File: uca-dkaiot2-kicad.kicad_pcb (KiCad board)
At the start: 2 copper layers, 73 x 77.5 mm, 184 parts, among them J1 Conn_01x04, J10 Conn_Coaxial, J11 Conn_01x02, J12 Conn_01x02, J20 Conn_01x01, J21 Conn_01x01, J22 Conn_01x01, J23 Conn_01x01, J24 Conn_01x01, J25 Conn_01x01, J26 Conn_01x01, J2J14 Conn_02x06_Odd_Even, J3 Conn_01x02, J4 Conn_01x02, J5 Conn_01x02, J6 Conn_Coaxial, J7 Conn_01x05, J8 USB_B_Micro, J9J13 Conn_ARM_SWD_TagConnect_TC203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, U1 NCV8170AXV300T2G, U10 NCV8170AXV300T2G, U11 DRV5023AJxLPG, U12 R5478N101CD, U13 FDV301N, U14 FDV301N, U15 R5478N101CD, U16 FDV301N, U17 FDV301N, U18 LTR-303ALS-01, U19 ICM-20948, U2 Quectel_L96, U20 KXTJ3-1057, U21 HP203B, U22 SPH0645LM4H, U24 KX023-1025, U26 NCV8170BXV180T2G, U28 BSS138L, U29 SGP30, U3 Conn_01x04, U30 BSS138L, U31 BSS138L, U32 Micro_SD_Card_Det1, U33 NCV8170AXV300T2G, U4 STM32U595RITx, U5 E22-900M22S, U6 LSM303AH, U7 BME280, U8 ATECC608A-SSHDA, U9 MCP73831-2-OT, X1 SMD3225-4, X2 SMD2012-2

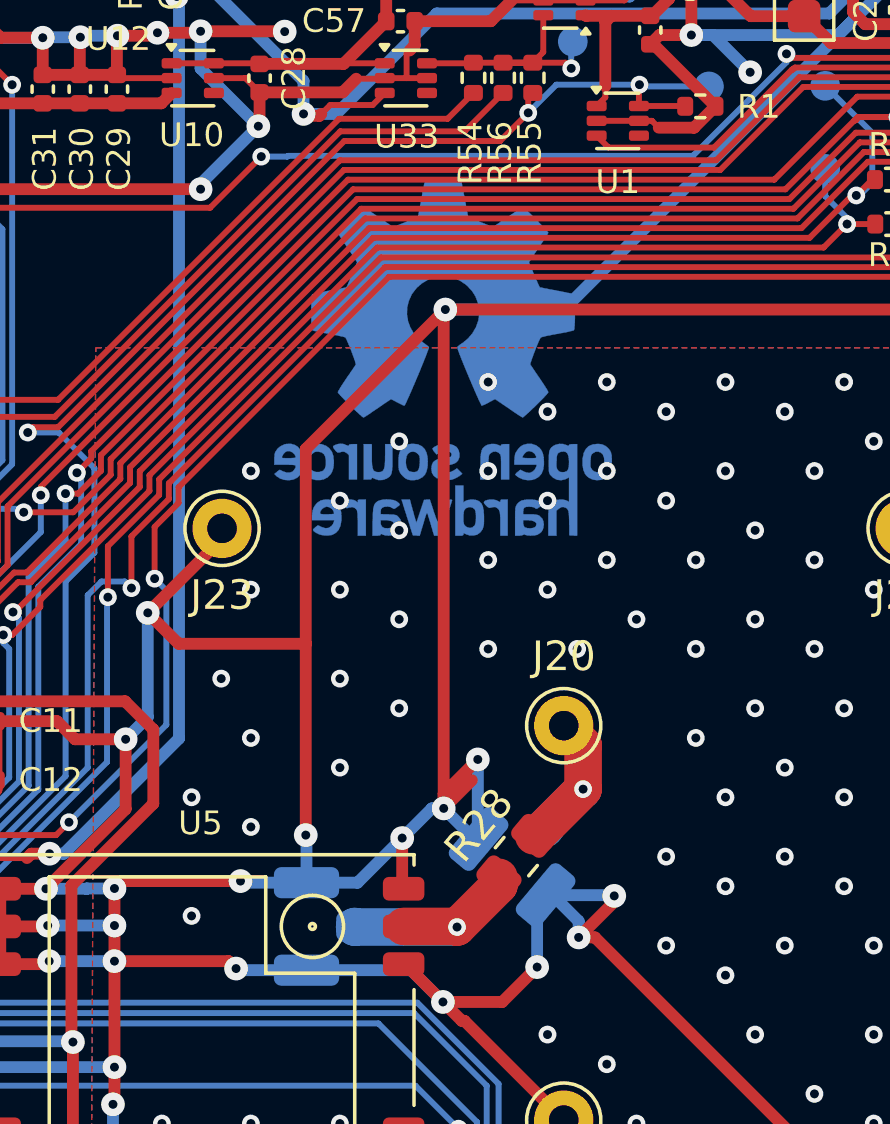
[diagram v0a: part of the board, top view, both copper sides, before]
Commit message: OSHW logo tied to ground net
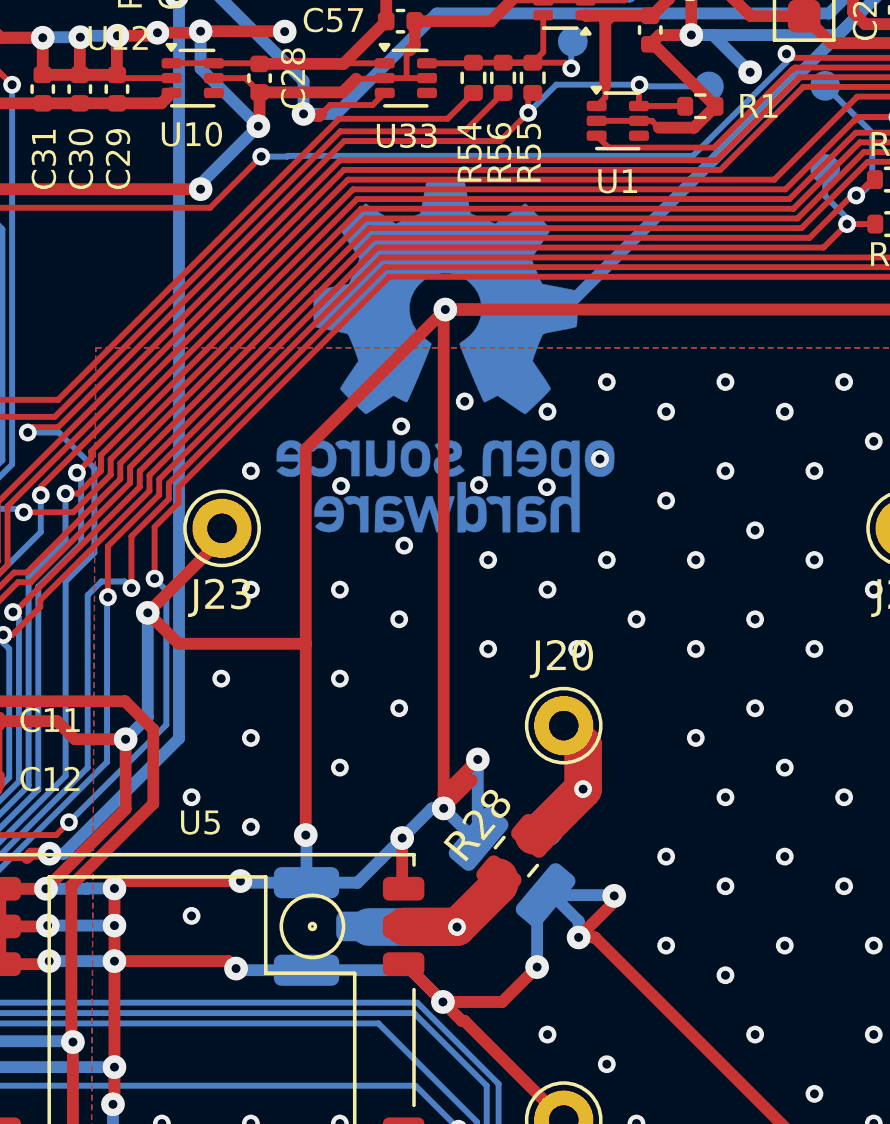
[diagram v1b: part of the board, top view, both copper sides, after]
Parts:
- moved SYM1 6.00 mm to (62.8, 48.8)

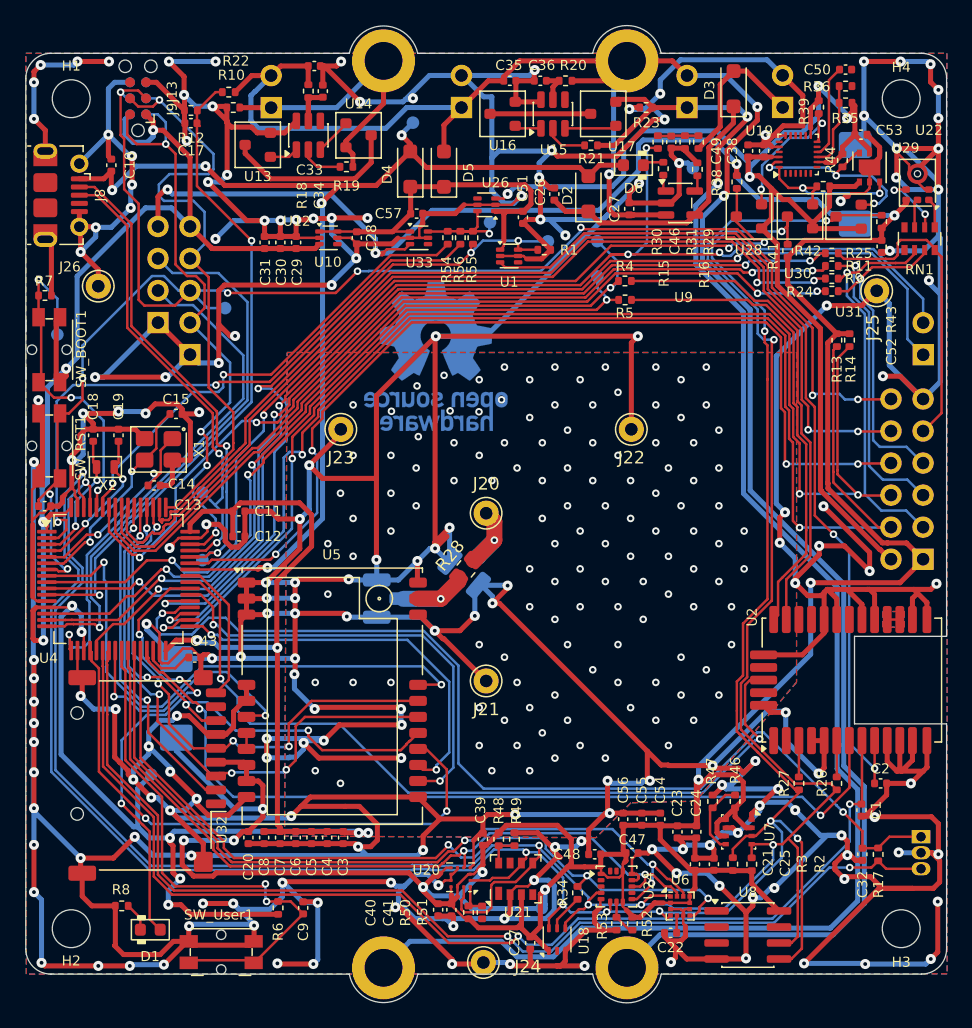
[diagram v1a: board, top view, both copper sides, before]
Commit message: v0.2: fix Ebyte E22-900M22S pinout
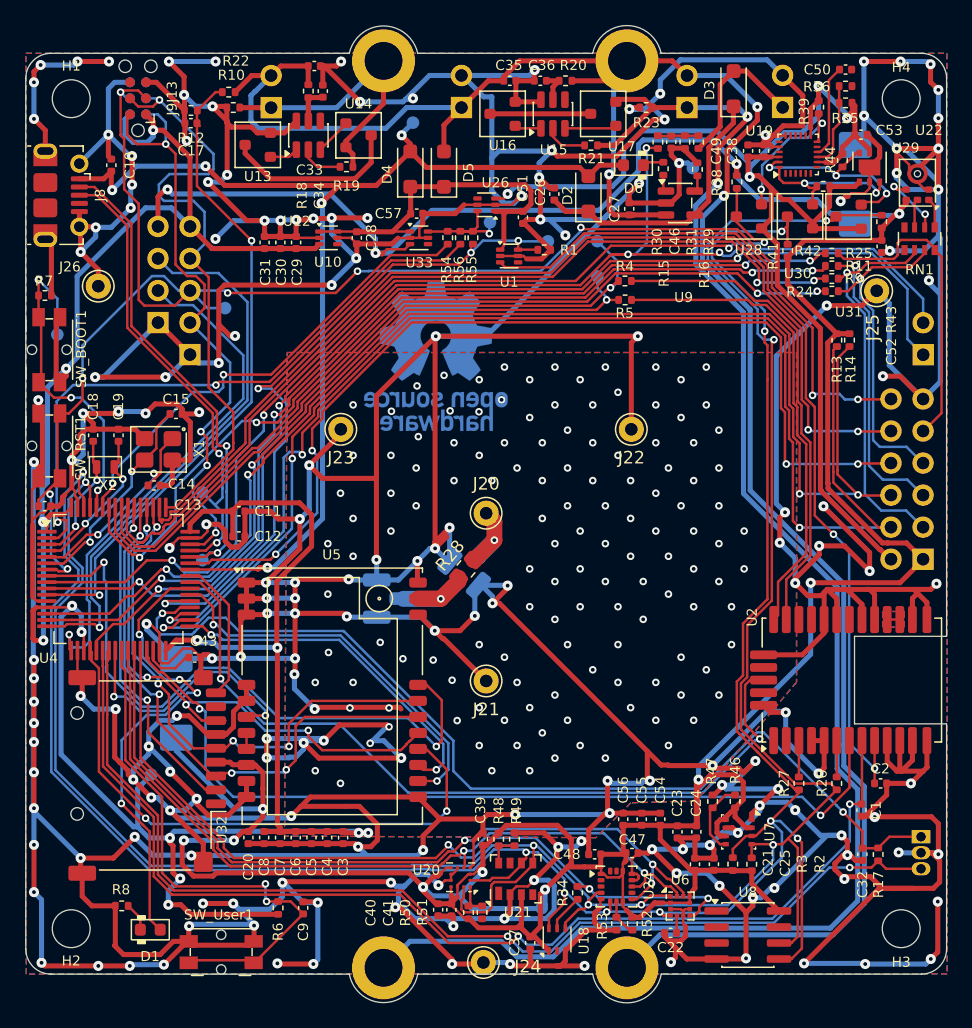
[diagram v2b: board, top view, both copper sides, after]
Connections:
- U5 pad 10: V_PERIPH_3V -> GND
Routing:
- net NSS_E22: track 45.2 -> 51.1 mm
- net DIO1_E22: track 35.5 -> 31.0 mm
- net BUSY_E22: track 31.4 -> 27.8 mm
- net GND: track 1368.3 -> 1371.6 mm, vias 312 -> 319
- net HALL_On_Off: track 82.2 -> 79.0 mm
- net V_PERIPH_3V: track 315.9 -> 316.6 mm
- net TIMEPULSE: track 64.5 -> 63.8 mm
- net INT_ACC_3: track 64.3 -> 63.7 mm
- net I2C1_SCL: track 198.2 -> 197.6 mm
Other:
- board text added: "UCA DKAIoT2 KiCad v0.2 //piernov"

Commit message: pcb: fix revision number text
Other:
- board text removed: "UCA DKAIoT2 KiCad v0.1 //piernov"
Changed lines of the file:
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@@
 		(layer "Edge.Cuts")
 	)
-	(gr_text "UCA DKAIoT2 KiCad\nv0.1\n//piernov"
+	(gr_text "UCA DKAIoT2 KiCad\nv0.2\n//piernov"
 		(at 74.3966 71.1708 0)
 		(layer "F.Mask")
@@
 			(justify bottom)
 		)
-		(render_cache "UCA DKAIoT2 KiCad\nv0.1\n//piernov" 0
+		(render_cache "UCA DKAIoT2 KiCad\nv0.2\n//piernov" 0
 			(polygon
 				(pts
@@
 			(polygon
 				(pts
-					(xy 75.279831 68.893591) (xy 75.279831 69.6908) (xy 75.122978 69.6908) (xy 75.122978 69.075014)
-					(xy 74.933934 69.135098) (xy 74.933934 69.011072) (xy 75.263467 68.893591)
-				)
-			)
+					(xy 75.44108 69.567848) (xy 75.44108 69.6908) (xy 74.89676 69.6908) (xy 74.89676 69.585873) (xy 75.154143 69.309439)
+					(xy 75.190293 69.266878) (xy 75.215351 69.23304) (xy 75.235427 69.200218) (xy 75.247884 69.173395)
+					(xy 75.255572 69.146919) (xy 75.257996 69.122739) (xy 75.254799 69.088258) (xy 75.24593 69.060653)
+					(xy 75.231014 69.037381) (xy 75.21071 69.020109) (xy 75.185606 69.009427) (xy 75.153606 69.005601)
+					(xy 75.119551 69.010222) (xy 75.091568 69.023479) (xy 75.068962 69.044486) (xy 75.052245 69.072719)
+					(xy 75.042333 69.105482) (xy 75.038861 69.143696) (xy 74.880885 69.143696) (xy 74.884719 69.097087)
+					(xy 74.896014 69.053726) (xy 74.914785 69.012928) (xy 74.940375 68.976042) (xy 74.972055 68.944533)
+					(xy 75.010431 68.918015) (xy 75.052916 68.898788) (xy 75.101337 68.886831) (xy 75.156879 68.882649)
+					(xy 75.212161 68.88596) (xy 75.258803 68.895243) (xy 75.298149 68.90976) (xy 75.334018 68.930811)
+					(xy 75.362891 68.956616) (xy 75.385588 68.987478) (xy 75.401784 69.022356) (xy 75.411858 69.062234)
+					(xy 75.415386 69.108134) (xy 75.412237 69.147053) (xy 75.402783 69.185021) (xy 75.387775 69.221905)
+					(xy 75.366977 69.259467) (xy 75.341876 69.295942) (xy 75.310996 69.334156) (xy 75.23831 69.412412)
+					(xy 75.100068 69.567848)
+				)
+			)
